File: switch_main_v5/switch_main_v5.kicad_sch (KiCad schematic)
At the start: 7 parts

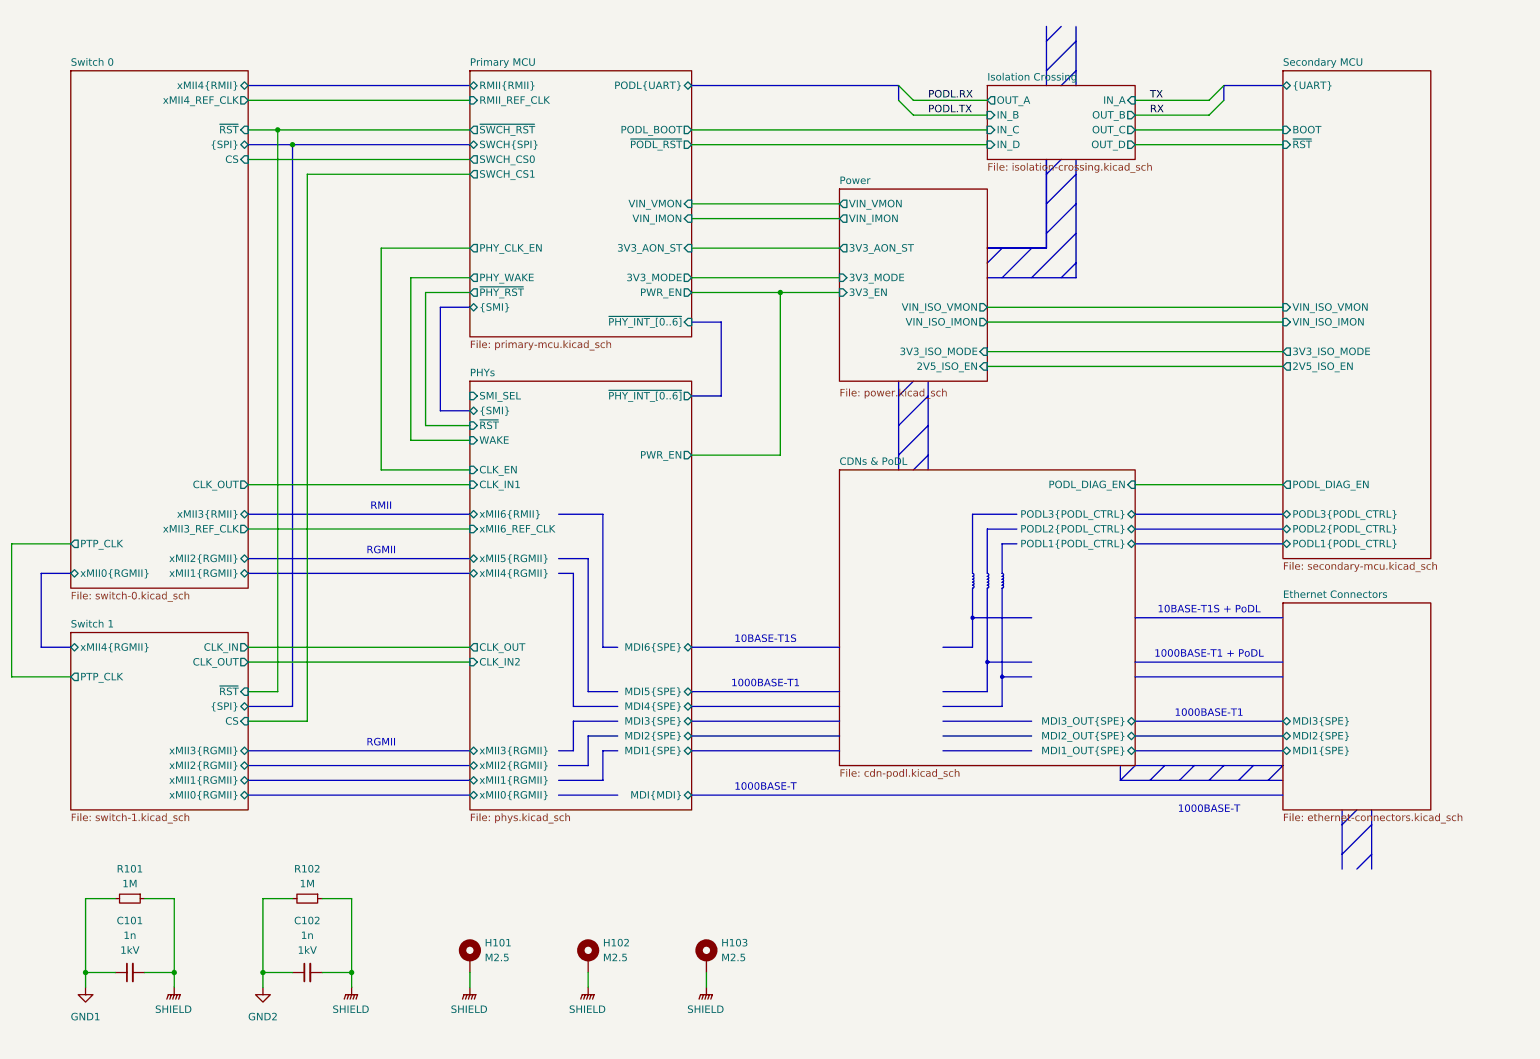
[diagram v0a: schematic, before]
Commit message: MDIO multiplexing
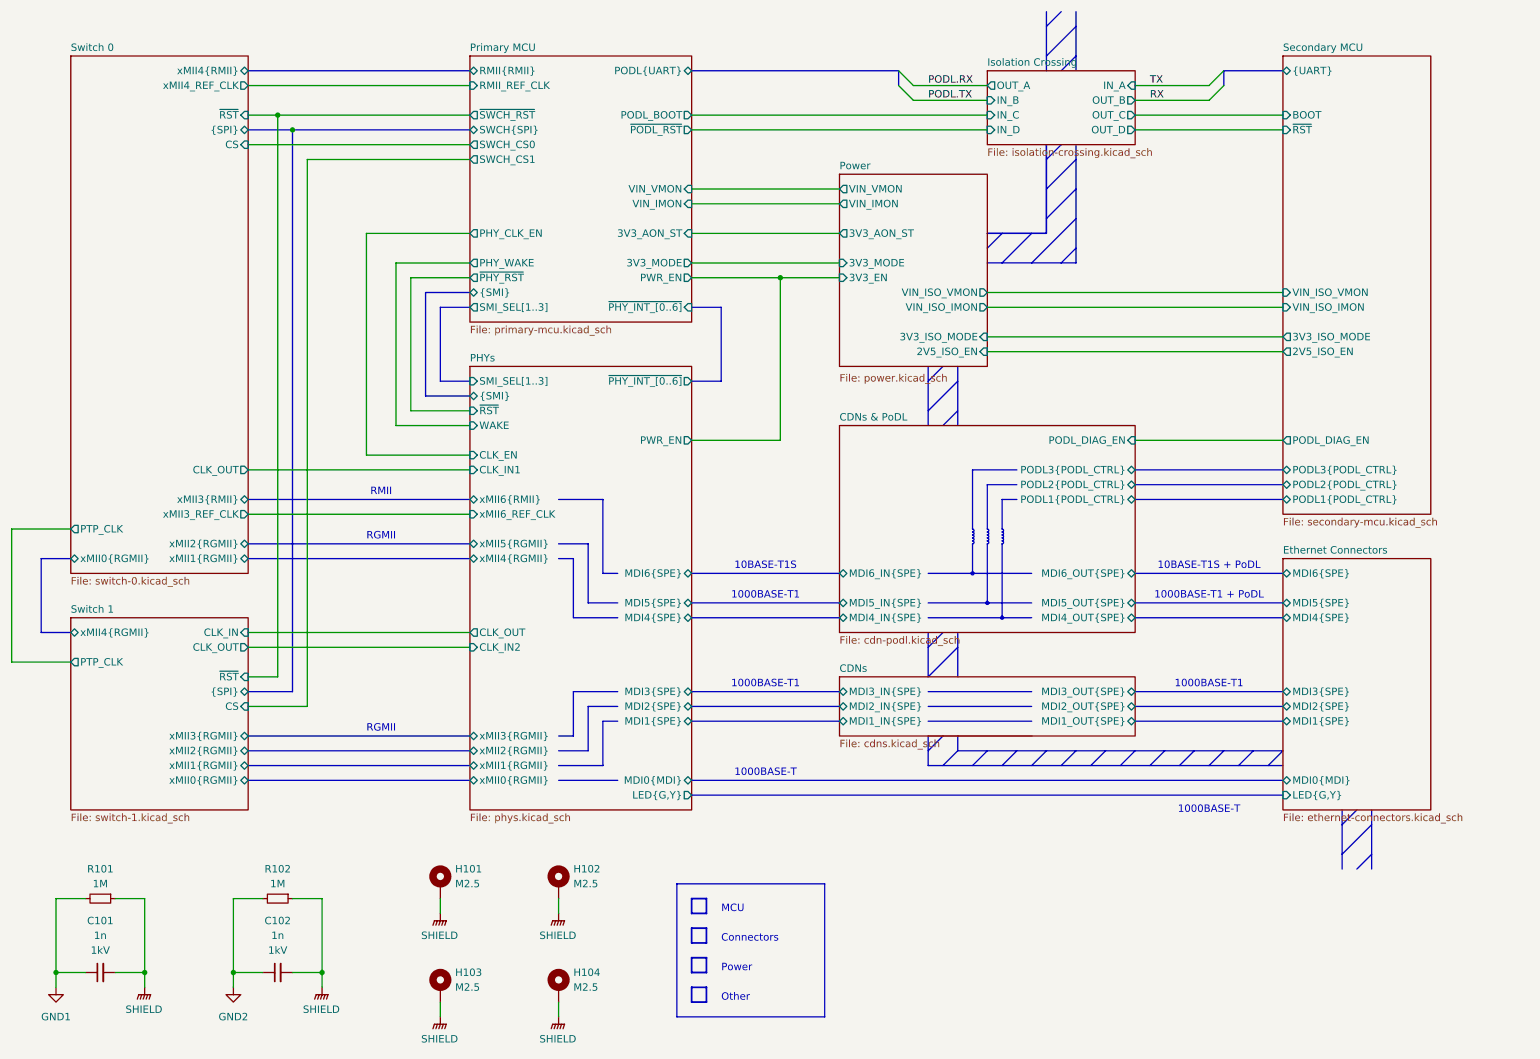
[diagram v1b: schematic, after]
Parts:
- added H104: M2.5, MountingHole:MountingHole_2.7mm_M2.5_Pad, symbol Mechanical:MountingHole_Pad
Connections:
- net SHIELD: now also H104.1
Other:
- added sheet CDNs (cdns.kicad_sch)
- sheet CDNs & PoDL ports: added MDI4_IN{SPE}, MDI4_OUT{SPE}, MDI5_IN{SPE}, MDI5_OUT{SPE}, MDI6_IN{SPE}, MDI6_OUT{SPE}; removed MDI1_OUT{SPE}, MDI2_OUT{SPE}, MDI3_OUT{SPE}
- sheet Ethernet Connectors ports: added LED{G,Y}, MDI0{MDI}, MDI4{SPE}, MDI5{SPE}, MDI6{SPE}; removed none
- sheet PHYs ports: added LED{G,Y}, MDI0{MDI}, SMI_SEL[1..3]; removed MDI{MDI}, SMI_SEL
- sheet Primary MCU ports: added SMI_SEL[1..3]; removed none
- note added: "Connectors"
- note added: "MCU"
- note added: "Other"
- note added: "Power"
- title: Switch V4 Top Level Schematic -> Switch V5 Top Level Schematic
- moved on the sheet: C101, C102, H101, H102, H103, R101, R102

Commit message: Updated 1v0_buck_converter feedback resistors
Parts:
- renumbered H103 to H102, H102 to H103
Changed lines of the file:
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@@
-		)
-	)
-	(text "1000BASE-T"
-		(exclude_from_sim no)
-		(at 228.6 152.4 0)
-		(effects
-			(font
-				(size 1.27 1.27)
-			)
 		)
 	)
@@
 		(at 96.52 165.1 0)
 		(unit 1)
-		(exclude_from_sim yes)
+		(exclude_from_sim no)
 		(in_bom no)
 		(on_board yes)
@@
 		(dnp no)
 		(fields_autoplaced yes)
-		(property "Reference" "#PWR0106"
+		(property "Reference" "#PWR0107"
 			(at 116.84 175.26 0)
 			(effects
@@
 			(project "switch_main_v4"
 				(path "/a5e57332-4284-4d3c-ab3c-13bc0ddb29b6"
-					(reference "#PWR0106")
+					(reference "#PWR0107")
 					(unit 1)
 				)
@@
 		(at 96.52 182.88 0)
 		(unit 1)
-		(exclude_from_sim yes)
+		(exclude_from_sim no)
 		(in_bom no)
 		(on_board yes)
 		(dnp no)
 		(fields_autoplaced yes)
-		(property "Reference" "H103"
+		(property "Reference" "H102"
 			(at 99.06 180.3399 0)
 			(effects
@@
 			(project "switch_main_v4"
 				(path "/a5e57332-4284-4d3c-ab3c-13bc0ddb29b6"
-					(reference "H103")
+					(reference "H102")
 					(unit 1)
 				)
@@
 		(at 116.84 182.88 0)
 		(unit 1)
-		(exclude_from_sim yes)
+		(exclude_from_sim no)
 		(in_bom no)
 		(on_board yes)
@@
 		(dnp no)
 		(fields_autoplaced yes)
-		(property "Reference" "#PWR0107"
+		(property "Reference" "#PWR0106"
 			(at 96.52 193.04 0)
 			(effects
@@
 			(project "switch_main_v4"
 				(path "/a5e57332-4284-4d3c-ab3c-13bc0ddb29b6"
-					(reference "#PWR0107")
+					(reference "#PWR0106")
 					(unit 1)
 				)
@@
 		(at 116.84 165.1 0)
 		(unit 1)
-		(exclude_from_sim yes)
+		(exclude_from_sim no)
 		(in_bom no)
 		(on_board yes)
 		(dnp no)
 		(fields_autoplaced yes)
-		(property "Reference" "H102"
+		(property "Reference" "H103"
 			(at 119.38 162.5599 0)
 			(effects
@@
 			(project "switch_main_v4"
 				(path "/a5e57332-4284-4d3c-ab3c-13bc0ddb29b6"
-					(reference "H102")
+					(reference "H103")
 					(unit 1)
 				)

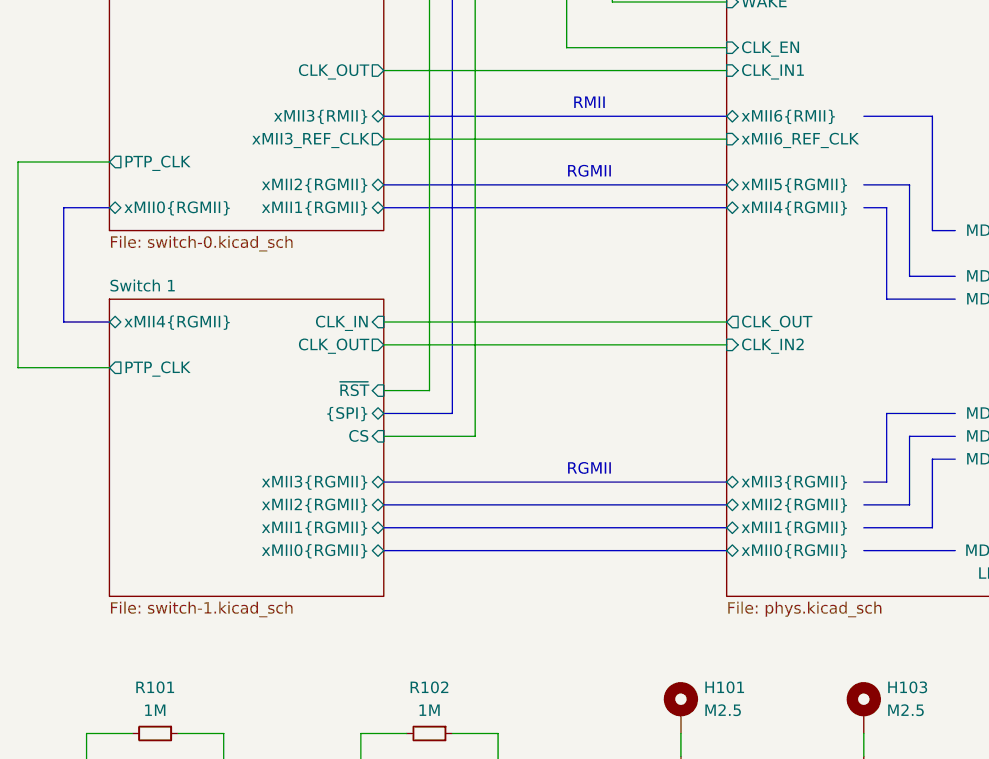
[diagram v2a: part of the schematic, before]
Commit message: Changed main 3V3 regulator to 3A, added switch 2 crystal & other changes
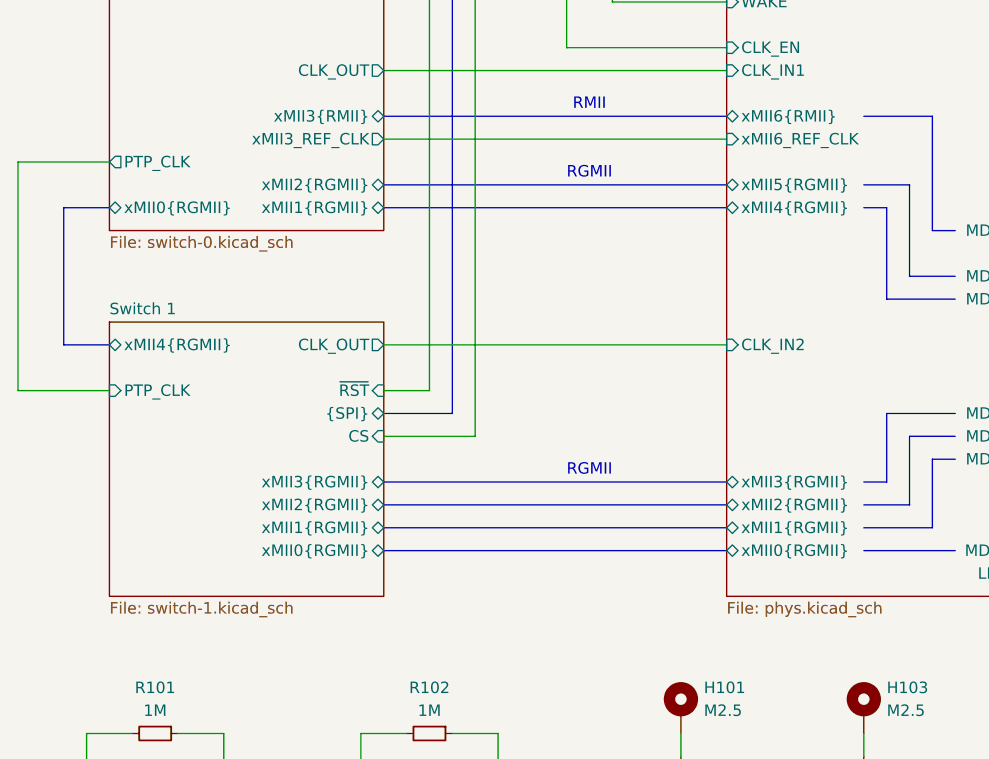
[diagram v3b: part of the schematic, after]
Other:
- sheet PHYs ports: added none; removed CLK_OUT
- sheet Switch 1 ports: added none; removed CLK_IN
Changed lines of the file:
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@@
 	(bus
 		(pts
-			(xy 27.94 121.92) (xy 27.94 109.22)
+			(xy 27.94 124.46) (xy 27.94 109.22)
 		)
 		(stroke
@@
 	(wire
 		(pts
-			(xy 22.86 104.14) (xy 22.86 127)
+			(xy 22.86 104.14) (xy 22.86 129.54)
 		)
 		(stroke
@@
 	(wire
 		(pts
-			(xy 22.86 127) (xy 33.02 127)
+			(xy 22.86 129.54) (xy 33.02 129.54)
 		)
 		(stroke
@@
 	(bus
 		(pts
-			(xy 33.02 121.92) (xy 27.94 121.92)
-		)
-		(stroke
-			(width 0)
-			(type default)
-		)
-	)
-	(wire
-		(pts
-			(xy 63.5 121.92) (xy 101.6 121.92)
+			(xy 33.02 124.46) (xy 27.94 124.46)
 		)
 		(stroke
@@
 	)
 	(sheet
-		(at 33.02 119.38)
-		(size 30.48 33.02)
+		(at 33.02 121.92)
+		(size 30.48 30.48)
 		(exclude_from_sim no)
 		(in_bom yes)
@@
 		)
 		(property "Sheetname" "Switch 1"
-			(at 33.02 118.6684 0)
+			(at 33.02 121.2084 0)
 			(effects
 				(font
@@
 			)
 		)
-		(pin "PTP_CLK" output
-			(at 33.02 127 180)
-			(effects
-				(font
-					(size 1.27 1.27)
-				)
-				(justify left)
-			)
-		)
 		(pin "{SPI}" bidirectional
 			(at 63.5 132.08 0)
@@
 		)
 		(pin "xMII4{RGMII}" bidirectional
-			(at 33.02 121.92 180)
+			(at 33.02 124.46 180)
 			(effects
 				(font
@@
 			)
 		)
-		(pin "CLK_IN" input
-			(at 63.5 121.92 0)
+		(pin "PTP_CLK" input
+			(at 33.02 129.54 180)
 			(effects
 				(font
 					(size 1.27 1.27)
 				)
-				(justify right)
+				(justify left)
 			)
 		)
@@
 			(effects
 				(font
-					(size 1.27 1.27)
-				)
-				(justify left)
-			)
-		)
-		(pin "CLK_OUT" output
-			(at 101.6 121.92 180)
-			(effects
-				(font

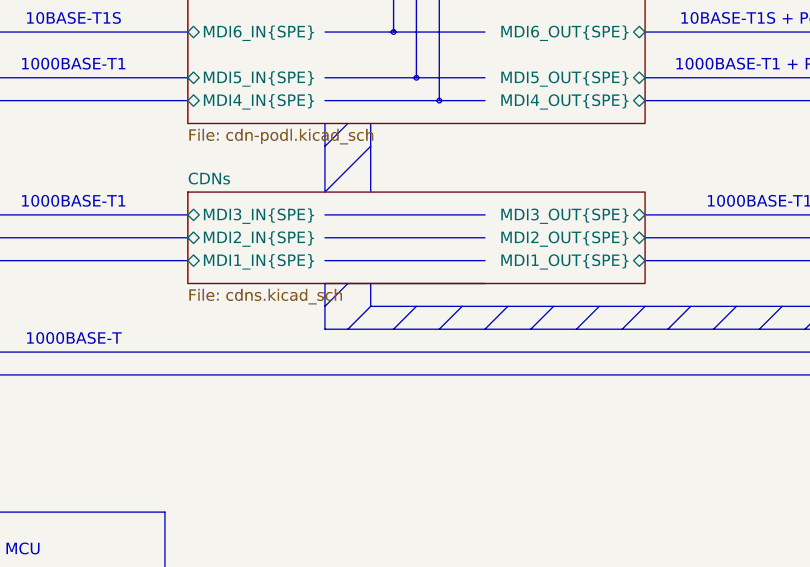
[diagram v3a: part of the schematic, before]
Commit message: PHY 1 & 2 routing progress and passive placement
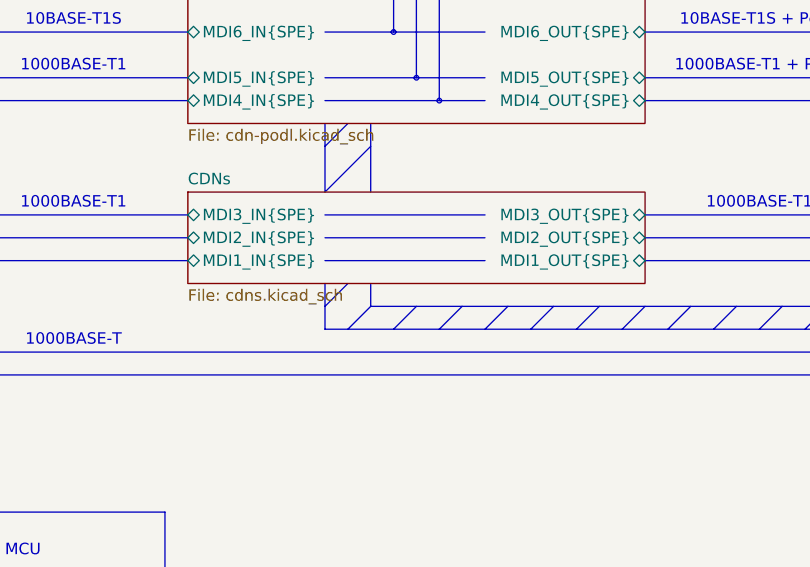
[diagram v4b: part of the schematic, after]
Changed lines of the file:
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@@
-		)
-	)
-	(polyline
-		(pts
-			(xy 180.34 139.7) (xy 198.12 139.7)
-		)
-		(stroke
-			(width 0)
-			(type default)
 		)
 	)

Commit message: Placed most remaining passives and test points
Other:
- sheet Switch 0 ports: added SS; removed CS
- sheet Switch 1 ports: added SS; removed CS
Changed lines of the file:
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@@
-			)
-		)
-		(pin "CS" input
-			(at 63.5 134.62 0)
-			(effects
-				(font
-					(size 1.27 1.27)
-				)
-				(justify right)
 			)
 		)
@@
 				)
 				(justify left)
+			)
+		)
+		(pin "SS" input
+			(at 63.5 134.62 0)
+			(effects
+				(font
+					(size 1.27 1.27)
+				)
+				(justify right)
 			)
 		)
@@
 			)
 		)
-		(pin "CS" input
+		(pin "SS" input
 			(at 63.5 38.1 0)
 			(effects

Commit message: Tidied schematic and PCB
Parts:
- renumbered H103 to H102, H102 to H103
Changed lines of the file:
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@@
 		(dnp no)
 		(fields_autoplaced yes)
-		(property "Reference" "#PWR0101"
+		(property "Reference" "#PWR0103"
 			(at 30.48 189.23 0)
 			(effects
@@
 			(project "switch_main_v4"
 				(path "/a5e57332-4284-4d3c-ab3c-13bc0ddb29b6"
-					(reference "#PWR0101")
+					(reference "#PWR0103")
 					(unit 1)
 				)
@@
 		(dnp no)
 		(fields_autoplaced yes)
-		(property "Reference" "#PWR0102"
+		(property "Reference" "#PWR0104"
 			(at 45.72 187.96 0)
 			(effects
@@
 			(project "switch_main_v4"
 				(path "/a5e57332-4284-4d3c-ab3c-13bc0ddb29b6"
-					(reference "#PWR0102")
+					(reference "#PWR0104")
 					(unit 1)
 				)
@@
 		(dnp no)
 		(fields_autoplaced yes)
-		(property "Reference" "#PWR0104"
+		(property "Reference" "#PWR0106"
 			(at 76.2 187.96 0)
 			(effects
@@
 			(project "switch_main_v4"
 				(path "/a5e57332-4284-4d3c-ab3c-13bc0ddb29b6"
-					(reference "#PWR0104")
+					(reference "#PWR0106")
 					(unit 1)
 				)
@@
 		(dnp no)
 		(fields_autoplaced yes)
-		(property "Reference" "#PWR0107"
+		(property "Reference" "#PWR0102"
 			(at 116.84 175.26 0)
 			(effects
@@
 			(project "switch_main_v4"
 				(path "/a5e57332-4284-4d3c-ab3c-13bc0ddb29b6"
-					(reference "#PWR0107")
+					(reference "#PWR0102")
 					(unit 1)
 				)
@@
 		(dnp no)
 		(fields_autoplaced yes)
-		(property "Reference" "H102"
+		(property "Reference" "H103"
 			(at 99.06 180.3399 0)
 			(effects
@@
 			(project "switch_main_v4"
 				(path "/a5e57332-4284-4d3c-ab3c-13bc0ddb29b6"
-					(reference "H102")
+					(reference "H103")
 					(unit 1)
 				)
@@
 		(dnp no)
 		(fields_autoplaced yes)
-		(property "Reference" "#PWR0103"
+		(property "Reference" "#PWR0105"
 			(at 60.96 189.23 0)
 			(effects
@@
 			(project "switch_main_v4"
 				(path "/a5e57332-4284-4d3c-ab3c-13bc0ddb29b6"
-					(reference "#PWR0103")
+					(reference "#PWR0105")
 					(unit 1)
 				)
@@
 		(dnp no)
 		(fields_autoplaced yes)
-		(property "Reference" "#PWR0106"
+		(property "Reference" "#PWR0107"
 			(at 96.52 193.04 0)
 			(effects
@@
 			(project "switch_main_v4"
 				(path "/a5e57332-4284-4d3c-ab3c-13bc0ddb29b6"
-					(reference "#PWR0106")
+					(reference "#PWR0107")
 					(unit 1)
 				)
@@
 		(dnp no)
 		(fields_autoplaced yes)
-		(property "Reference" "#PWR0105"
+		(property "Reference" "#PWR0101"
 			(at 96.52 175.26 0)
 			(effects
@@
 			(project "switch_main_v4"
 				(path "/a5e57332-4284-4d3c-ab3c-13bc0ddb29b6"
-					(reference "#PWR0105")
+					(reference "#PWR0101")
 					(unit 1)
 				)
@@
 		(dnp no)
 		(fields_autoplaced yes)
-		(property "Reference" "H103"
+		(property "Reference" "H102"
 			(at 119.38 162.5599 0)
 			(effects
@@
 			(project "switch_main_v4"
 				(path "/a5e57332-4284-4d3c-ab3c-13bc0ddb29b6"
-					(reference "H103")
+					(reference "H102")
 					(unit 1)
 				)
@@
 			(project "switch_main_v5"
 				(path "/a5e57332-4284-4d3c-ab3c-13bc0ddb29b6"
-					(page "17")
+					(page "26")
 				)
 			)
@@
 			(project "switch_main_v5"
 				(path "/a5e57332-4284-4d3c-ab3c-13bc0ddb29b6"
-					(page "29")
+					(page "16")
 				)
 			)
@@
 			(project "switch_main_v5"
 				(path "/a5e57332-4284-4d3c-ab3c-13bc0ddb29b6"
-					(page "9")
+					(page "15")
 				)
 			)
@@
 			(project "switch_main_v5"
 				(path "/a5e57332-4284-4d3c-ab3c-13bc0ddb29b6"
-					(page "10")
+					(page "17")
 				)
 			)
@@
 			(project "switch_main_v5"
 				(path "/a5e57332-4284-4d3c-ab3c-13bc0ddb29b6"
-					(page "24")
+					(page "36")
 				)
 			)
@@
 			(project "switch_main_v5"
 				(path "/a5e57332-4284-4d3c-ab3c-13bc0ddb29b6"
-					(page "8")
+					(page "14")
 				)
 			)
@@
 			(project "switch_main_v5"
 				(path "/a5e57332-4284-4d3c-ab3c-13bc0ddb29b6"
-					(page "25")
+					(page "37")
 				)
 			)
@@
 			(project "switch_main_v5"
 				(path "/a5e57332-4284-4d3c-ab3c-13bc0ddb29b6"
-					(page "26")
-				)
-			)
+					(page "38")
+				)
+			)
